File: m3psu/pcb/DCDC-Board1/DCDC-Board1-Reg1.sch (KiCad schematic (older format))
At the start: 36 parts

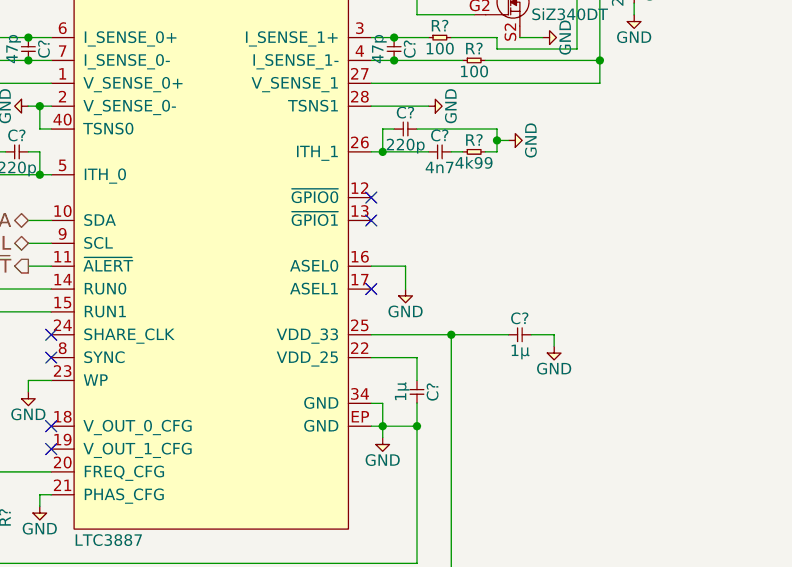
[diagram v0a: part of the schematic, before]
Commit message: Minor changes for uniformity for DC/DC converters.
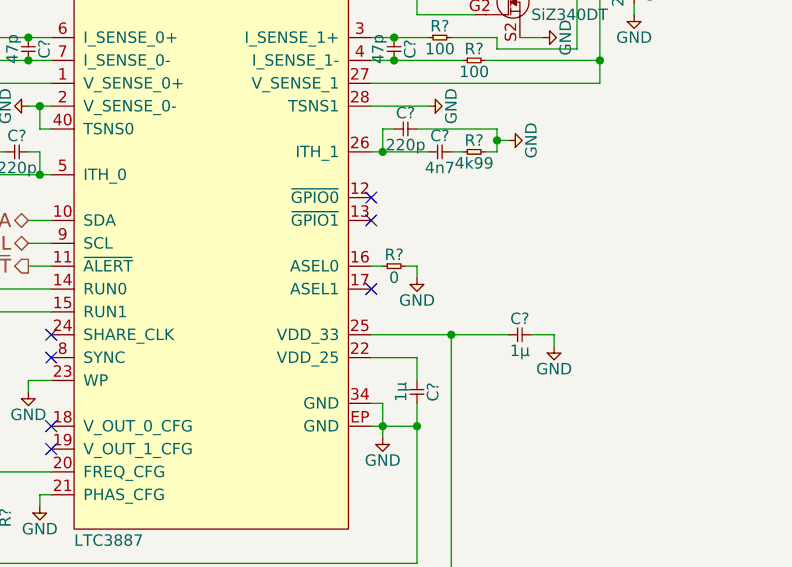
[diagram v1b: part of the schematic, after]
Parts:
- added R?: 0, agg:0402, symbol R
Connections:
- net GND: now also R?.2; no longer IC?.16 (ASEL0)
- new net: IC?.16 (ASEL0), R?.1
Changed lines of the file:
@@
 EESchema Schematic File Version 2
 LIBS:agg-kicad
-LIBS:m3psu-cache
+LIBS:DCDC-Board1-cache
 EELAYER 25 0
 EELAYER END
 $Descr A4 11693 8268
 encoding utf-8
-Sheet 6 13
+Sheet 3 3
 Title ""
 Date ""
@@
 L GND #PWR?
 U 1 1 56D53955
-P 6750 4500
-F 0 "#PWR?" H 6620 4540 50  0001 L CNN
-F 1 "GND" H 6750 4400 50  0000 C CNN
-F 2 "" H 6750 4500 60  0000 C CNN
-F 3 "" H 6750 4500 60  0000 C CNN
-	1    6750 4500
+P 6800 4450
+F 0 "#PWR?" H 6670 4490 50  0001 L CNN
+F 1 "GND" H 6800 4350 50  0000 C CNN
+F 2 "" H 6800 4450 60  0000 C CNN
+F 3 "" H 6800 4450 60  0000 C CNN
+	1    6800 4450
 	1    0    0    -1
 $EndComp
@@
 Wire Wire Line
 	5100 4200 5200 4200
-Wire Wire Line
-	6600 4400 6750 4400
-Wire Wire Line
-	6750 4400 6750 4500
 Wire Wire Line
 	5100 4900 5100 4950
@@
 	-1   0    0    -1
 $EndComp
+$Comp
+L R R?
+U 1 1 56E1FCB4
+P 6650 4400
+F 0 "R?" H 6700 4450 50  0000 C CNN
+F 1 "0" H 6700 4350 50  0000 C CNN
+F 2 "agg:0402" H 6650 4400 50  0001 C CNN
+F 3 "" H 6650 4400 50  0001 C CNN
+F 4 "2502491" H 6650 4400 60  0001 C CNN "Farnell"
+	1    6650 4400
+	1    0    0    -1
+$EndComp
+Wire Wire Line
+	6600 4400 6650 4400
+Wire Wire Line
+	6750 4400 6800 4400
+Wire Wire Line
+	6800 4400 6800 4450
 $EndSCHEMATC

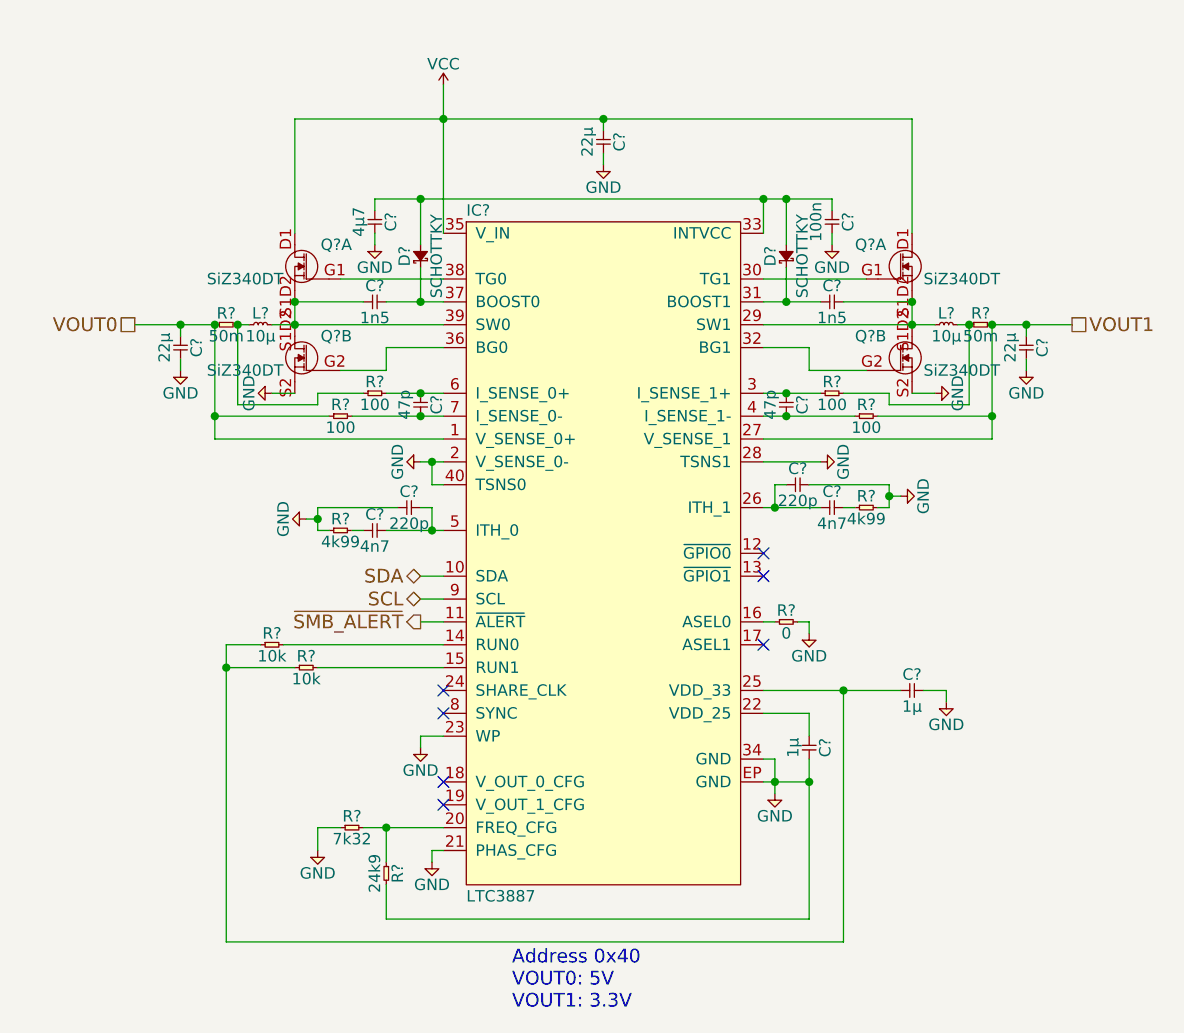
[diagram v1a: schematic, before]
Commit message: create DCDC1/2/3 from prototype
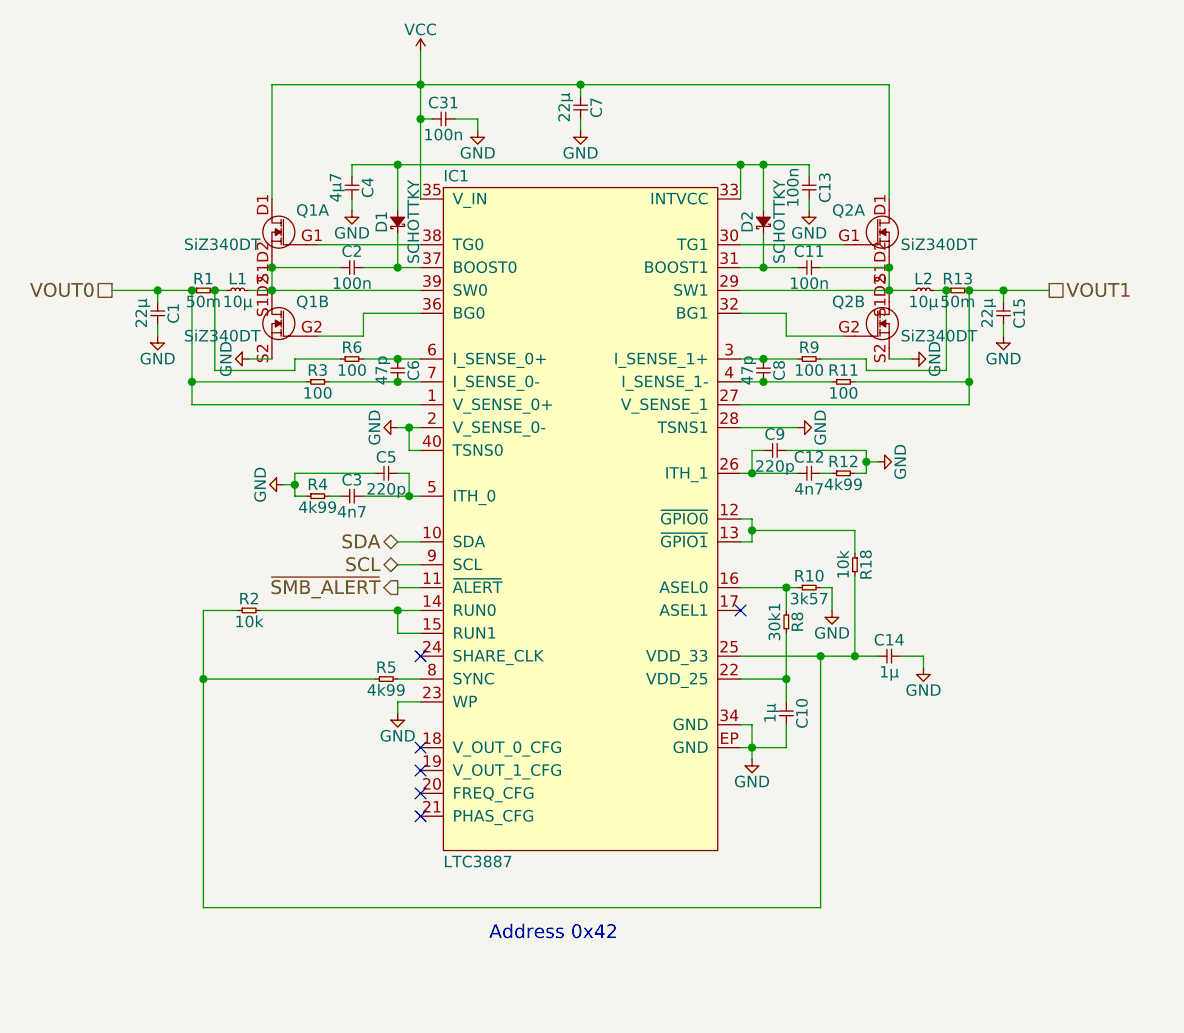
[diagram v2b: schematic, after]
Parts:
- removed C? (x2): 1n5, agg:0402, symbol C
- removed C?: 4µ7, agg:0603, symbol C
- removed C? (x3): 22µ, agg:0805, symbol C
- removed C? (x2): 47p, agg:0402, symbol C
- removed C? (x2): 1µ, agg:0402, symbol C
- removed C?: 100n, agg:0402, symbol C
- removed C? (x2): 4n7, agg:0402, symbol C
- removed C? (x2): 220p, agg:0402, symbol C
- removed D? (x2): SCHOTTKY, agg:0603-LED, symbol SCHOTTKY
- removed IC?: LTC3887, agg:QFN-40-EP-LTC-UJ, symbol LTC3887
- removed L? (x2): 10µ, agg:TYS5040, symbol L
- removed Q? (x4): SiZ340DT, agg:PowerPair3x3, symbol SiZ340DT
- removed R? (x2): 50m, agg:0603, symbol R
- removed R? (x4): 100, agg:0402, symbol R
- removed R?: 24k9, agg:0402, symbol R
- removed R?: 7k32, agg:0402, symbol R
- removed R? (x2): 4k99, agg:0402, symbol R
- removed R? (x2): 10k, agg:0402, symbol R
- removed R?: 0, agg:0402, symbol R
- added C1, C15, C7: 22µ, agg:0805, symbol C
- added C10, C14: 1µ, agg:0402, symbol C
- added C11, C13, C2, C31: 100n, agg:0402, symbol C
- added C12, C3: 4n7, agg:0402, symbol C
- added C4: 4µ7, agg:0402, symbol C
- added C5, C9: 220p, agg:0402, symbol C
- added C6, C8: 47p, agg:0402, symbol C
- added D1, D2: SCHOTTKY, agg:0603-LED, symbol SCHOTTKY
- added IC1: LTC3887, agg:QFN-40-EP-LTC-UJ, symbol LTC3887
- added L1, L2: 10µ, agg:TYS5040, symbol L
- added Q1, Q2: SiZ340DT, agg:PowerPair3x3, symbol SiZ340DT
- added R1, R13: 50m, agg:0603, symbol R
- added R10: 3k57, agg:0402, symbol R
- added R11, R3, R6, R9: 100, agg:0402, symbol R
- added R12, R4, R5: 4k99, agg:0402, symbol R
- added R18, R2: 10k, agg:0402, symbol R
- added R8: 30k1, agg:0402, symbol R
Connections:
- net GND: now also C1.2, C10.2, C13.2, C14.2, C15.2, C31.2, C4.2, C5.1, C7.2, C9.2, IC1.2 (V_SENSE_0-), IC1.23 (WP), IC1.28 (TSNS1), IC1.34 (GND), IC1.40 (TSNS0), IC1.EP (GND), Q1.S2, Q2.S2, R10.2, R12.2, R4.1
- net SCL: now also IC1.9 (SCL)
- net SDA: now also IC1.10 (SDA)
- net VCC: now also C31.1, C7.1, IC1.35 (V_IN), Q1.D1 (S1D2), Q2.D1 (S1D2)
- net VOUT0: now also C1.1, IC1.1 (V_SENSE_0+), R1.1, R3.1
- net VOUT1: now also C15.1, IC1.27 (V_SENSE_1), R11.2, R13.2
- net ~SMB_ALERT: now also IC1.11 (~ALERT)
- new net: IC1.12 (~GPIO0), IC1.13 (~GPIO1), R18.1
- new net: IC1.14 (RUN0), IC1.15 (RUN1), R2.2
- new net: IC1.16 (ASEL0), R10.1, R8.1
- new net: C10.1, IC1.22 (VDD_25), R8.2
- new net: C14.1, IC1.25 (VDD_33), R18.2, R2.1, R5.1
- new net: C12.1, C9.1, IC1.26 (ITH_1)
- new net: C11.2, IC1.29 (SW1), L2.1, Q2.S1D2, Q2.S1D2
- new net: C8.1, IC1.3 (I_SENSE_1+), R9.1
- new net: IC1.30 (TG1), Q2.G1
- new net: C11.1, D2.1, IC1.31 (BOOST1)
- new net: IC1.32 (BG1), Q2.G2
- new net: C13.1, C4.1, D1.2, D2.2, IC1.33 (INTVCC)
- new net: IC1.36 (BG0), Q1.G2
- new net: C2.2, D1.1, IC1.37 (BOOST0)
- new net: IC1.38 (TG0), Q1.G1
- new net: C2.1, IC1.39 (SW0), L1.2, Q1.S1D2, Q1.S1D2
- new net: C8.2, IC1.4 (I_SENSE_1-), R11.1
- new net: C3.2, C5.2, IC1.5 (ITH_0)
- new net: C6.1, IC1.6 (I_SENSE_0+), R6.2
- new net: C6.2, IC1.7 (I_SENSE_0-), R3.2
- new net: IC1.8 (SYNC), R5.2
- new net: L2.2, R13.1, R9.2
- new net: L1.1, R1.2, R6.1
- new net: C12.2, R12.1
- new net: C3.1, R4.2
- no-connect marks 7 -> 6
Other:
- note added: "Address 0x42"
- note removed: "Address 0x40\nVOUT0: 5V\nVOUT1: 3.3V"

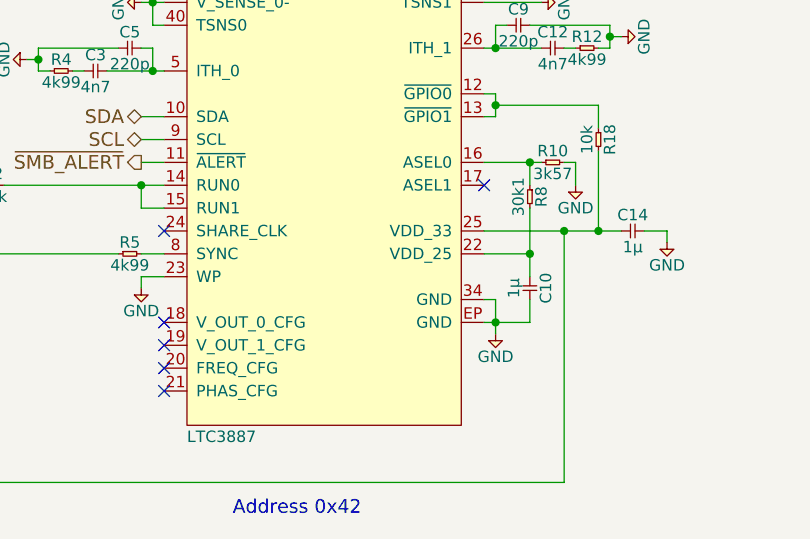
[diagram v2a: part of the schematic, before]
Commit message: update DCDC address setting resistors due to making DCDC2 with DCDC1's resistors (intentionally)
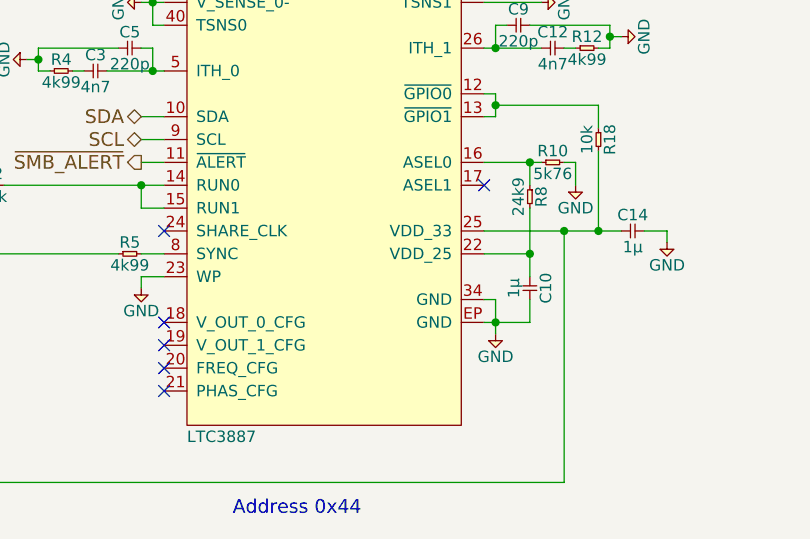
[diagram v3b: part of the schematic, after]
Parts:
- R10: value 3k57 -> 5k76
- R8: value 30k1 -> 24k9
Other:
- note added: "Address 0x44"
- note removed: "Address 0x42"
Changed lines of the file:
@@
 P 6750 4250
 F 0 "R10" H 6800 4300 50  0000 C CNN
-F 1 "3k57" H 6800 4200 50  0000 C CNN
+F 1 "5k76" H 6800 4200 50  0000 C CNN
 F 2 "agg:0402" H 6750 4250 50  0001 C CNN
 F 3 "" H 6750 4250 50  0001 C CNN
@@
 P 6700 4350
 F 0 "R8" H 6750 4400 50  0000 C CNN
-F 1 "30k1" H 6750 4300 50  0000 C CNN
+F 1 "24k9" H 6750 4300 50  0000 C CNN
 F 2 "agg:0402" H 6700 4350 50  0001 C CNN
 F 3 "" H 6700 4350 50  0001 C CNN
@@
 ~SMB_ALERT
 Text Notes 5400 5800 0    60   ~ 0
-Address 0x42
+Address 0x44
 Wire Wire Line
 	5000 4750 5100 4750
